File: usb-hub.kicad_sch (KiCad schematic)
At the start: 24 parts, among them U4 USB2422-I_MJ, Y1 Oscillator_24MHz_ESC_2016MV

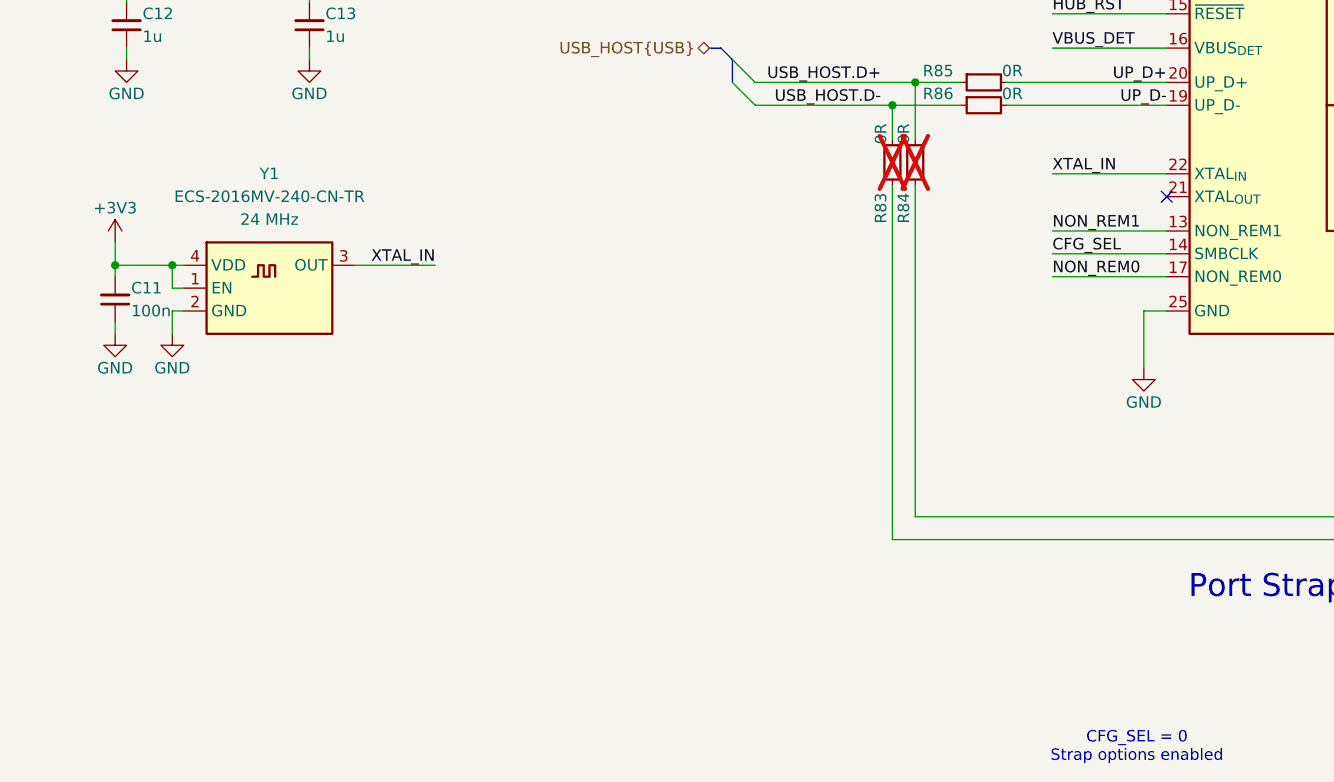
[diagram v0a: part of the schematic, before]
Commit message: [#83767] Replace USB Hub clk generator with crystal to align with reference design
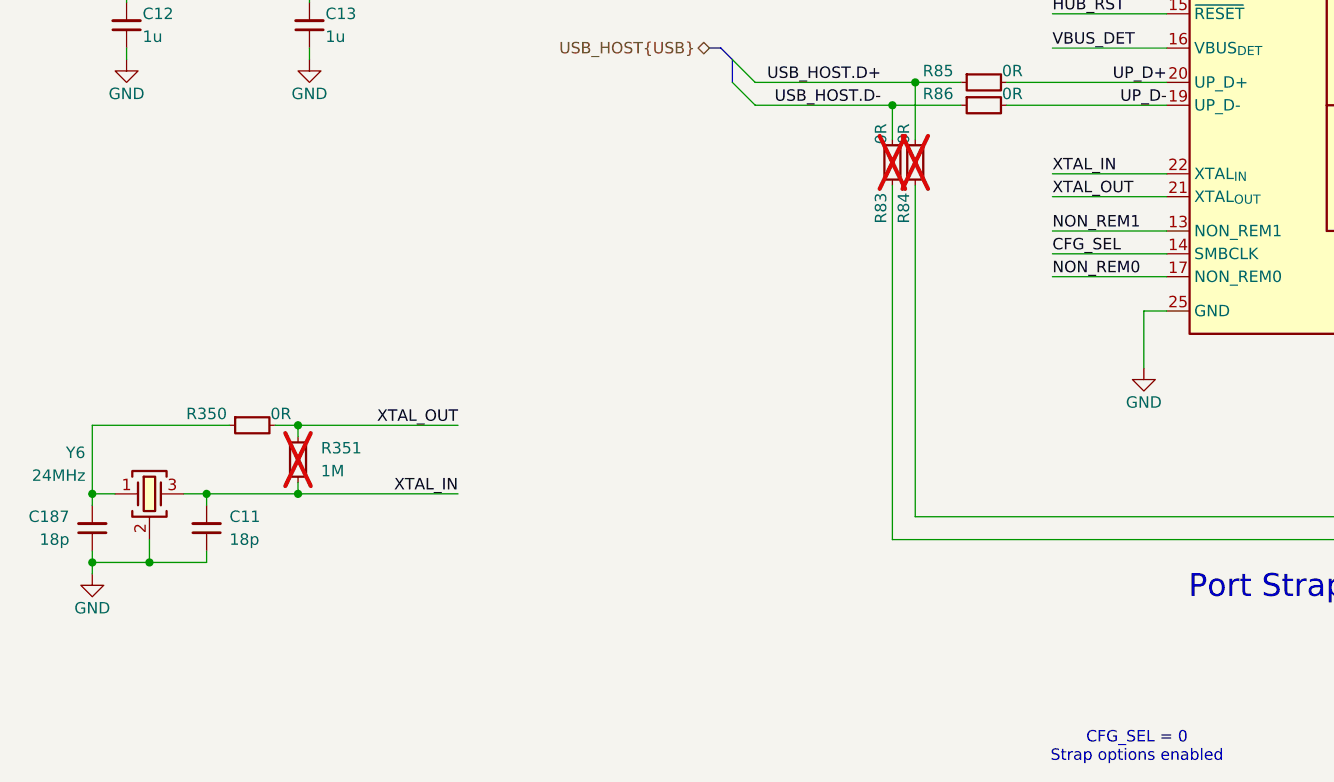
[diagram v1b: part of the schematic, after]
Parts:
- removed C11: C_100n_0402, antmicro-footprints:C_0402_1005Metric, symbol antmicroCapacitors0402:C_100n_0402
- removed Y1: Oscillator_24MHz_ESC_2016MV, antmicro-footprints:Oscillator_SMD_ECS_2016MV_2x1.6x0.85mm, symbol antmicroOscillators:Oscillator_24MHz_ESC_2016MV
- added C11, C187: C_18p_0402, antmicro-footprints:C_0402_1005Metric, symbol antmicroCapacitors0402:C_18p_0402
- added R350: R_0R_0402, antmicro-footprints:R_0402_1005Metric, symbol antmicroResistors0402:R_0R_0402
- added R351: R_1M_0402, antmicro-footprints:R_0402_1005Metric, symbol antmicroResistors0402:R_1M_0402
- added Y6: Resonator_27.12MHz_XRCGB, antmicro-footprints:Resonator_SMD_Murata_XRCGB_2x1.6x0.65mm, symbol antmicroResonators:Resonator_24MHz_XRCGB
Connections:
- net GND: now also C11.1, C187.1, Y6.2 (SH), Y6.4 (SH)
- net XTAL_IN: now also C11.2, R351.1, Y6.3
- net XTAL_OUT: now reaches U4.21 (XTAL_{OUT})
- net XTAL_OUT: now also R350.2, R351.2
- new net: C187.2, R350.1, Y6.1
- no-connect marks 3 -> 2
